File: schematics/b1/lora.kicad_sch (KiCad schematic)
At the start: 4 parts, among them U1 Ai-Thinker-Ra-02

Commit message: Updated annotations.
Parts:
- renumbered C14 to C10, C12 to C8, C13 to C9, U1 to U5
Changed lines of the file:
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@@
   (title_block
     (title "LoRa")
-    (date "2024-02-06")
+    (date "2024-02-15")
     (rev "1")
     (company "shawnd.xyz")
@@
   (symbol (lib_id "Device:C") (at 88.9 41.91 0) (unit 1)
     (in_bom yes) (on_board yes) (dnp no)
-    (property "Reference" "C14" (at 92.71 40.64 0)
+    (property "Reference" "C10" (at 92.71 40.64 0)
       (effects (font (size 1.27 1.27)) (justify left))
     )
@@
       (project "b1"
         (path "/d6142fa5-2354-4512-9919-37616259c364/bca829a9-1cbe-4403-a4e4-7724b6c8becd"
-          (reference "C14") (unit 1)
+          (reference "C10") (unit 1)
         )
       )
@@
   (symbol (lib_id "power:GND") (at 99.06 80.01 0) (unit 1)
     (in_bom yes) (on_board yes) (dnp no) (fields_autoplaced)
-    (property "Reference" "#PWR02" (at 99.06 86.36 0)
+    (property "Reference" "#PWR020" (at 99.06 86.36 0)
       (effects (font (size 1.27 1.27)) hide)
     )
@@
       (project "b1"
         (path "/d6142fa5-2354-4512-9919-37616259c364/bca829a9-1cbe-4403-a4e4-7724b6c8becd"
-          (reference "#PWR02") (unit 1)
+          (reference "#PWR020") (unit 1)
         )
       )
@@
   (symbol (lib_id "power:GND") (at 64.77 48.26 0) (unit 1)
     (in_bom yes) (on_board yes) (dnp no) (fields_autoplaced)
-    (property "Reference" "#PWR01" (at 64.77 54.61 0)
+    (property "Reference" "#PWR019" (at 64.77 54.61 0)
       (effects (font (size 1.27 1.27)) hide)
     )
@@
       (project "b1"
         (path "/d6142fa5-2354-4512-9919-37616259c364/bca829a9-1cbe-4403-a4e4-7724b6c8becd"
-          (reference "#PWR01") (unit 1)
+          (reference "#PWR019") (unit 1)
         )
       )
@@
   (symbol (lib_id "Device:C_Polarized") (at 64.77 41.91 0) (unit 1)
     (in_bom yes) (on_board yes) (dnp no)
-    (property "Reference" "C12" (at 68.58 40.64 0)
+    (property "Reference" "C8" (at 68.58 40.64 0)
       (effects (font (size 1.27 1.27)) (justify left))
     )
@@
       (project "b1"
         (path "/d6142fa5-2354-4512-9919-37616259c364/bca829a9-1cbe-4403-a4e4-7724b6c8becd"
-          (reference "C12") (unit 1)
+          (reference "C8") (unit 1)
         )
       )
@@
   (symbol (lib_id "RF_Module:Ai-Thinker-Ra-02") (at 99.06 64.77 0) (unit 1)
     (in_bom yes) (on_board yes) (dnp no) (fields_autoplaced)
-    (property "Reference" "U1" (at 101.2541 46.99 0)
+    (property "Reference" "U5" (at 101.2541 46.99 0)
       (effects (font (size 1.27 1.27)) (justify left))
     )
@@
       (project "b1"
         (path "/d6142fa5-2354-4512-9919-37616259c364/bca829a9-1cbe-4403-a4e4-7724b6c8becd"
-          (reference "U1") (unit 1)
+          (reference "U5") (unit 1)
         )
       )
@@
   (symbol (lib_id "Device:C") (at 77.47 41.91 0) (unit 1)
     (in_bom yes) (on_board yes) (dnp no) (fields_autoplaced)
-    (property "Reference" "C13" (at 81.28 40.64 0)
+    (property "Reference" "C9" (at 81.28 40.64 0)
       (effects (font (size 1.27 1.27)) (justify left))
     )
@@
       (project "b1"
         (path "/d6142fa5-2354-4512-9919-37616259c364/bca829a9-1cbe-4403-a4e4-7724b6c8becd"
-          (reference "C13") (unit 1)
-        )
-      )
+          (reference "C9") (unit 1)
+        )
+      )

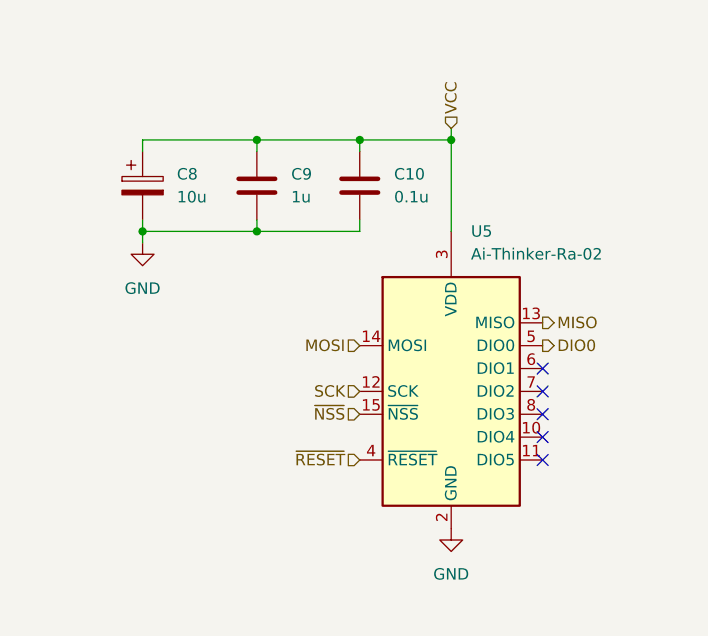
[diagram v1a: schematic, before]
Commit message: Wired LoRa and added a bulk to the status block.
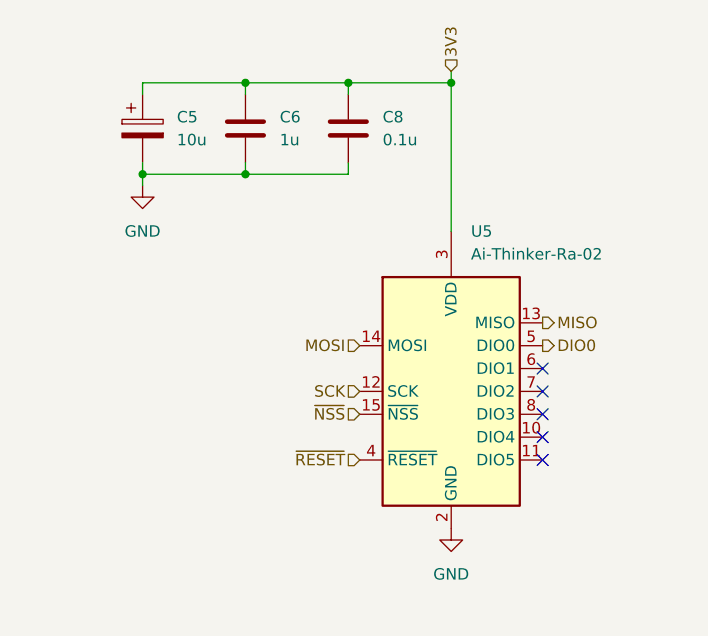
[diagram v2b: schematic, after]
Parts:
- removed C10: 0.1u, symbol Device:C
- removed C8: 10u, symbol Device:C_Polarized
- removed C9: 1u, symbol Device:C
- added C5: 10u, symbol Device:C_Polarized
- added C6: 1u, symbol Device:C
- added C8: 0.1u, symbol Device:C
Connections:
- net GND: now also C5.2, C6.2, C8.2
- net VCC renamed 3V3
- net 3V3: now also C5.1, C6.1, C8.1
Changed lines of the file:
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@@
     (comment 4 "The LoRa block is just an AI Thinker RA-02 LoRa module. This is used for backup")
   )
-  (junction (at 77.47 46.99) (diameter 0) (color 0 0 0 0)
-  )
-  (junction (at 99.06 36.83) (diameter 0) (color 0 0 0 0)
-  )
-  (junction (at 64.77 46.99) (diameter 0) (color 0 0 0 0)
-  )
-  (junction (at 77.47 36.83) (diameter 0) (color 0 0 0 0)
-  )
-  (junction (at 88.9 36.83) (diameter 0) (color 0 0 0 0)
+  (junction (at 99.06 30.48) (diameter 0) (color 0 0 0 0)
+  )
+  (junction (at 76.2 30.48) (diameter 0) (color 0 0 0 0)
+  )
+  (junction (at 76.2 40.64) (diameter 0) (color 0 0 0 0)
+  )
+  (junction (at 87.63 30.48) (diameter 0) (color 0 0 0 0)
+  )
+  (junction (at 64.77 40.64) (diameter 0) (color 0 0 0 0)
   )
   (no_connect (at 109.22 72.39))
@@
   (no_connect (at 109.22 64.77))
   (no_connect (at 109.22 69.85))
-  (wire (pts (xy 77.47 46.99) (xy 88.9 46.99))
-    (stroke (width 0) (type default))
-  )
-  (wire (pts (xy 77.47 46.99) (xy 77.47 45.72))
-    (stroke (width 0) (type default))
-  )
-  (wire (pts (xy 88.9 36.83) (xy 88.9 38.1))
-    (stroke (width 0) (type default))
-  )
-  (wire (pts (xy 88.9 46.99) (xy 88.9 45.72))
-    (stroke (width 0) (type default))
-  )
-  (wire (pts (xy 64.77 45.72) (xy 64.77 46.99))
-    (stroke (width 0) (type default))
-  )
-  (wire (pts (xy 88.9 36.83) (xy 77.47 36.83))
-    (stroke (width 0) (type default))
-  )
-  (wire (pts (xy 64.77 38.1) (xy 64.77 36.83))
-    (stroke (width 0) (type default))
-  )
-  (wire (pts (xy 88.9 36.83) (xy 99.06 36.83))
-    (stroke (width 0) (type default))
-  )
-  (wire (pts (xy 99.06 46.99) (xy 99.06 36.83))
-    (stroke (width 0) (type default))
-  )
-  (wire (pts (xy 64.77 48.26) (xy 64.77 46.99))
-    (stroke (width 0) (type default))
-  )
-  (wire (pts (xy 99.06 35.56) (xy 99.06 36.83))
-    (stroke (width 0) (type default))
-  )
-  (wire (pts (xy 77.47 36.83) (xy 77.47 38.1))
-    (stroke (width 0) (type default))
-  )
-  (wire (pts (xy 64.77 46.99) (xy 77.47 46.99))
-    (stroke (width 0) (type default))
-  )
-  (wire (pts (xy 64.77 36.83) (xy 77.47 36.83))
+  (wire (pts (xy 99.06 30.48) (xy 99.06 46.99))
+    (stroke (width 0) (type default))
+  )
+  (wire (pts (xy 64.77 39.37) (xy 64.77 40.64))
+    (stroke (width 0) (type default))
+  )
+  (wire (pts (xy 87.63 30.48) (xy 76.2 30.48))
+    (stroke (width 0) (type default))
+  )
+  (wire (pts (xy 64.77 41.91) (xy 64.77 40.64))
+    (stroke (width 0) (type default))
+  )
+  (wire (pts (xy 99.06 30.48) (xy 87.63 30.48))
+    (stroke (width 0) (type default))
+  )
+  (wire (pts (xy 64.77 31.75) (xy 64.77 30.48))
+    (stroke (width 0) (type default))
+  )
+  (wire (pts (xy 87.63 40.64) (xy 87.63 39.37))
+    (stroke (width 0) (type default))
+  )
+  (wire (pts (xy 64.77 30.48) (xy 76.2 30.48))
+    (stroke (width 0) (type default))
+  )
+  (wire (pts (xy 64.77 40.64) (xy 76.2 40.64))
+    (stroke (width 0) (type default))
+  )
+  (wire (pts (xy 99.06 29.21) (xy 99.06 30.48))
+    (stroke (width 0) (type default))
+  )
+  (wire (pts (xy 76.2 40.64) (xy 87.63 40.64))
+    (stroke (width 0) (type default))
+  )
+  (wire (pts (xy 76.2 40.64) (xy 76.2 39.37))
+    (stroke (width 0) (type default))
+  )
+  (wire (pts (xy 87.63 30.48) (xy 87.63 31.75))
+    (stroke (width 0) (type default))
+  )
+  (wire (pts (xy 76.2 30.48) (xy 76.2 31.75))
     (stroke (width 0) (type default))
   )
@@
     (effects (font (size 1.27 1.27)) (justify right))
   )
-  (hierarchical_label "VCC" (shape input) (at 99.06 35.56 90) (fields_autoplaced)
-    (effects (font (size 1.27 1.27)) (justify left))
-  )
   (hierarchical_label "~{NSS}" (shape input) (at 88.9 67.31 180) (fields_autoplaced)
     (effects (font (size 1.27 1.27)) (justify right))
@@
     (effects (font (size 1.27 1.27)) (justify right))
   )
-  (symbol (lib_id "Device:C") (at 88.9 41.91 0) (unit 1)
-    (in_bom yes) (on_board yes) (dnp no)
-    (property "Reference" "C10" (at 92.71 40.64 0)
-      (effects (font (size 1.27 1.27)) (justify left))
-    )
-    (property "Value" "0.1u" (at 92.71 43.18 0)
-      (effects (font (size 1.27 1.27)) (justify left))
-    )
-    (property "Footprint" "" (at 89.8652 45.72 0)
-      (effects (font (size 1.27 1.27)) hide)
-    )
-    (property "Datasheet" "~" (at 88.9 41.91 0)
-      (effects (font (size 1.27 1.27)) hide)
-    )
-    (pin "2")
-    (pin "1")
-    (instances
-      (project "b1"
-        (path "/d6142fa5-2354-4512-9919-37616259c364/bca829a9-1cbe-4403-a4e4-7724b6c8becd"
-          (reference "C10") (unit 1)
-        )
-      )
-    )
+  (hierarchical_label "3V3" (shape input) (at 99.06 29.21 90) (fields_autoplaced)
+    (effects (font (size 1.27 1.27)) (justify left))
   )
   (symbol (lib_id "power:GND") (at 99.06 80.01 0) (unit 1)
@@
     )
   )
-  (symbol (lib_id "power:GND") (at 64.77 48.26 0) (unit 1)
-    (in_bom yes) (on_board yes) (dnp no) (fields_autoplaced)
-    (property "Reference" "#PWR019" (at 64.77 54.61 0)
-      (effects (font (size 1.27 1.27)) hide)
-    )
-    (property "Value" "GND" (at 64.77 53.34 0)
-      (effects (font (size 1.27 1.27)))
-    )
-    (property "Footprint" "" (at 64.77 48.26 0)
-      (effects (font (size 1.27 1.27)) hide)
-    )
-    (property "Datasheet" "" (at 64.77 48.26 0)
-      (effects (font (size 1.27 1.27)) hide)
-    )
-    (pin "1")
-    (instances
-      (project "b1"
-        (path "/d6142fa5-2354-4512-9919-37616259c364/bca829a9-1cbe-4403-a4e4-7724b6c8becd"
-          (reference "#PWR019") (unit 1)
-        )
-      )
-    )
-  )
-  (symbol (lib_id "Device:C_Polarized") (at 64.77 41.91 0) (unit 1)
+  (symbol (lib_id "Device:C") (at 87.63 35.56 0) (unit 1)
     (in_bom yes) (on_board yes) (dnp no)
-    (property "Reference" "C8" (at 68.58 40.64 0)
-      (effects (font (size 1.27 1.27)) (justify left))
-    )
-    (property "Value" "10u" (at 68.58 43.18 0)
-      (effects (font (size 1.27 1.27)) (justify left))
-    )
-    (property "Footprint" "" (at 65.7352 45.72 0)
-      (effects (font (size 1.27 1.27)) hide)
-    )
-    (property "Datasheet" "~" (at 64.77 41.91 0)
+    (property "Reference" "C8" (at 91.44 34.29 0)
+      (effects (font (size 1.27 1.27)) (justify left))
+    )
+    (property "Value" "0.1u" (at 91.44 36.83 0)
+      (effects (font (size 1.27 1.27)) (justify left))
+    )
+    (property "Footprint" "" (at 88.5952 39.37 0)
+      (effects (font (size 1.27 1.27)) hide)
+    )
+    (property "Datasheet" "~" (at 87.63 35.56 0)
       (effects (font (size 1.27 1.27)) hide)
     )
@@
     )
   )
-  (symbol (lib_id "Device:C") (at 77.47 41.91 0) (unit 1)
-    (in_bom yes) (on_board yes) (dnp no) (fields_autoplaced)
-    (property "Reference" "C9" (at 81.28 40.64 0)
-      (effects (font (size 1.27 1.27)) (justify left))
-    )
-    (property "Value" "1u" (at 81.28 43.18 0)
-      (effects (font (size 1.27 1.27)) (justify left))
-    )
-    (property "Footprint" "" (at 78.4352 45.72 0)
-      (effects (font (size 1.27 1.27)) hide)
-    )
-    (property "Datasheet" "~" (at 77.47 41.91 0)
-      (effects (font (size 1.27 1.27)) hide)
-    )
-    (pin "2")
-    (pin "1")
-    (instances
-      (project "b1"
-        (path "/d6142fa5-2354-4512-9919-37616259c364/bca829a9-1cbe-4403-a4e4-7724b6c8becd"
-          (reference "C9") (unit 1)
-        )
-      )
+  (symbol (lib_id "Device:C") (at 76.2 35.56 0) (unit 1)
+    (in_bom yes) (on_board yes) (dnp no) (fields_autoplaced)
+    (property "Reference" "C6" (at 80.01 34.29 0)
+      (effects (font (size 1.27 1.27)) (justify left))
+    )
+    (property "Value" "1u" (at 80.01 36.83 0)
+      (effects (font (size 1.27 1.27)) (justify left))
+    )
+    (property "Footprint" "" (at 77.1652 39.37 0)
+      (effects (font (size 1.27 1.27)) hide)
+    )
+    (property "Datasheet" "~" (at 76.2 35.56 0)
+      (effects (font (size 1.27 1.27)) hide)
+    )
+    (pin "2")
+    (pin "1")
+    (instances
+      (project "b1"
+        (path "/d6142fa5-2354-4512-9919-37616259c364/bca829a9-1cbe-4403-a4e4-7724b6c8becd"
+          (reference "C6") (unit 1)
+        )
+      )
+    )
+  )
+  (symbol (lib_id "Device:C_Polarized") (at 64.77 35.56 0) (unit 1)
+    (in_bom yes) (on_board yes) (dnp no)
+    (property "Reference" "C5" (at 68.58 34.29 0)
+      (effects (font (size 1.27 1.27)) (justify left))
+    )
+    (property "Value" "10u" (at 68.58 36.83 0)
+      (effects (font (size 1.27 1.27)) (justify left))
+    )
+    (property "Footprint" "" (at 65.7352 39.37 0)
+      (effects (font (size 1.27 1.27)) hide)
+    )
+    (property "Datasheet" "~" (at 64.77 35.56 0)
+      (effects (font (size 1.27 1.27)) hide)
+    )
+    (pin "2")
+    (pin "1")
+    (instances
+      (project "b1"
+        (path "/d6142fa5-2354-4512-9919-37616259c364/bca829a9-1cbe-4403-a4e4-7724b6c8becd"
+          (reference "C5") (unit 1)
+        )
+      )
+    )
+  )
+  (symbol (lib_id "power:GND") (at 64.77 41.91 0) (unit 1)
+    (in_bom yes) (on_board yes) (dnp no) (fields_autoplaced)
+    (property "Reference" "#PWR010" (at 64.77 48.26 0)
+      (effects (font (size 1.27 1.27)) hide)
+    )
+    (property "Value" "GND" (at 64.77 46.99 0)
+      (effects (font (size 1.27 1.27)))
+    )
+    (property "Footprint" "" (at 64.77 41.91 0)
+      (effects (font (size 1.27 1.27)) hide)
+    )
+    (property "Datasheet" "" (at 64.77 41.91 0)
+      (effects (font (size 1.27 1.27)) hide)
+    )
+    (pin "1")
+    (instances
+      (project "b1"
+        (path "/d6142fa5-2354-4512-9919-37616259c364/bca829a9-1cbe-4403-a4e4-7724b6c8becd"
+          (reference "#PWR010") (unit 1)
+        )
+      )
